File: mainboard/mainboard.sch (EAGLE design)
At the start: 54 parts, among them T2 NPN_BC817,215, U1 CD4051BM, X2 JST-XH-07-PIN-LONG-PAD

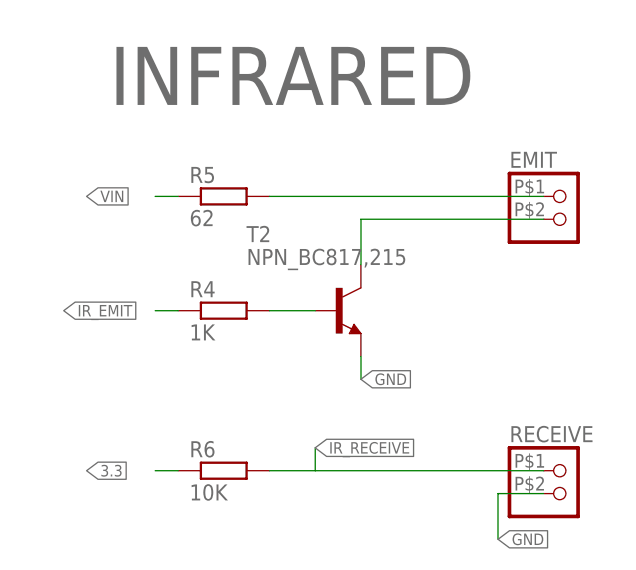
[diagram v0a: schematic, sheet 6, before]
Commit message: schematic modified on brushless board
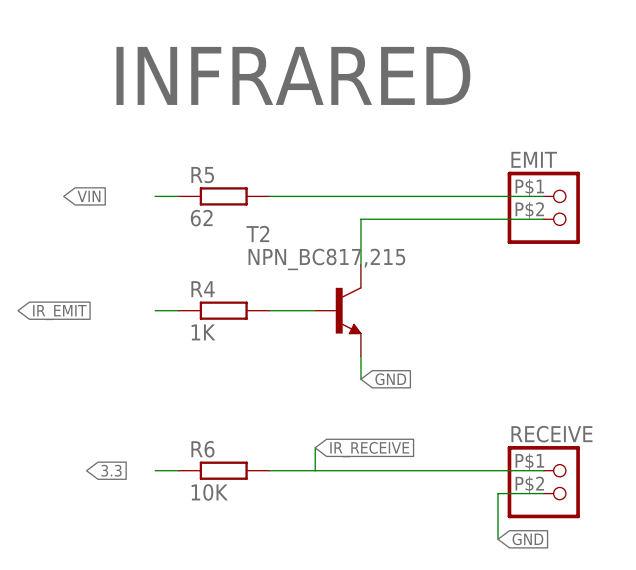
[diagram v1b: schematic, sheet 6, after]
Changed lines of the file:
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@@
 <layer number="91" name="Nets" color="2" fill="1" visible="yes" active="yes"/>
 <layer number="92" name="Busses" color="1" fill="1" visible="yes" active="yes"/>
-<layer number="93" name="Pins" color="2" fill="1" visible="yes" active="yes"/>
+<layer number="93" name="Pins" color="2" fill="1" visible="no" active="yes"/>
 <layer number="94" name="Symbols" color="4" fill="1" visible="yes" active="yes"/>
 <layer number="95" name="Names" color="7" fill="1" visible="yes" active="yes"/>
@@
 <pinref part="R5" gate="G$1" pin="1"/>
 <wire x1="-10.16" y1="15.24" x2="-12.7" y2="15.24" width="0.1524" layer="91"/>
-<label x="-20.32" y="15.24" size="1.27" layer="95" xref="yes"/>
+<label x="-22.86" y="15.24" size="1.27" layer="95" xref="yes"/>
 </segment>
 </net>
@@
 <pinref part="R4" gate="G$1" pin="1"/>
 <wire x1="-10.16" y1="2.54" x2="-12.7" y2="2.54" width="0.1524" layer="91"/>
-<label x="-22.86" y="2.54" size="1.27" layer="95" xref="yes"/>
-</segment>
-</net>
+<label x="-27.94" y="2.54" size="1.27" layer="95" xref="yes"/>
+</segment>
+</net>
